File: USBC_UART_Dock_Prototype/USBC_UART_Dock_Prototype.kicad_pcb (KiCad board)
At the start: 4 copper layers, 54.1 x 45.5 mm, 40 parts, among them J1 Conn_01x01, J2 Conn_01x01, J3 Conn_01x05_Socket, J4 USB4085-GF-A, U1 FT312D, U2 TPS25810, U3 TPD6S300A, U5 LP5907MFX-3.3/NOPB, Y1 12 MHz

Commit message: Ready for DFM
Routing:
- net /RTS: track 35.8 -> 31.1 mm
- net /CTS: track 34.7 -> 30.4 mm
- net /nPWR_FLT: track 32.0 -> 27.9 mm, vias 0 -> 2
- net /CONN_USB_CC2: track 12.3 -> 16.4 mm
- net GND: track 23.7 -> 27.2 mm
- net +3.3V: track 25.7 -> 22.2 mm, vias 23 -> 25
- net /nUSB_ERROR: track 44.3 -> 42.8 mm
- net +VUSB: track 5.74 -> 4.39 mm
- net Net-(U3-VBIAS): track 8.47 -> 7.48 mm, vias 2 -> 0
- net /nLD_DET: track 5.26 -> 5.97 mm
- net Net-(D5-A): track 4.28 -> 3.70 mm

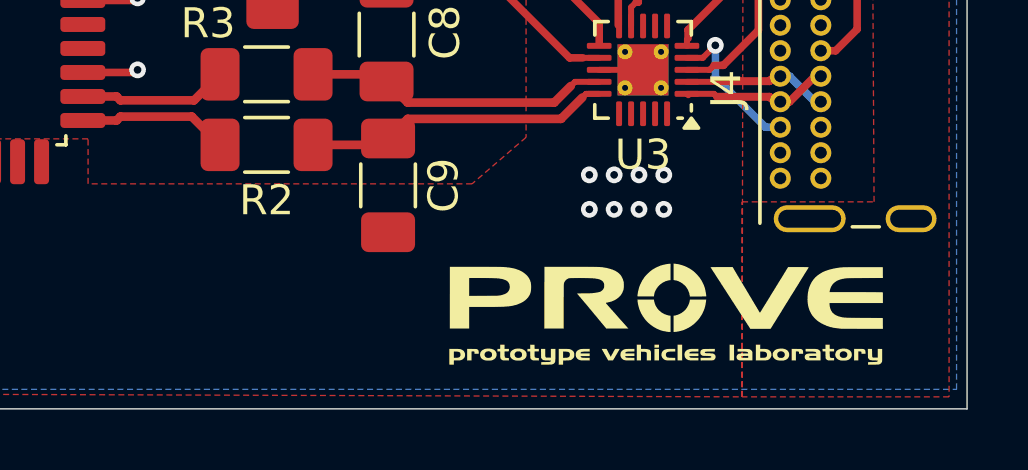
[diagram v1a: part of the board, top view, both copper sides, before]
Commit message: Add BAC logo
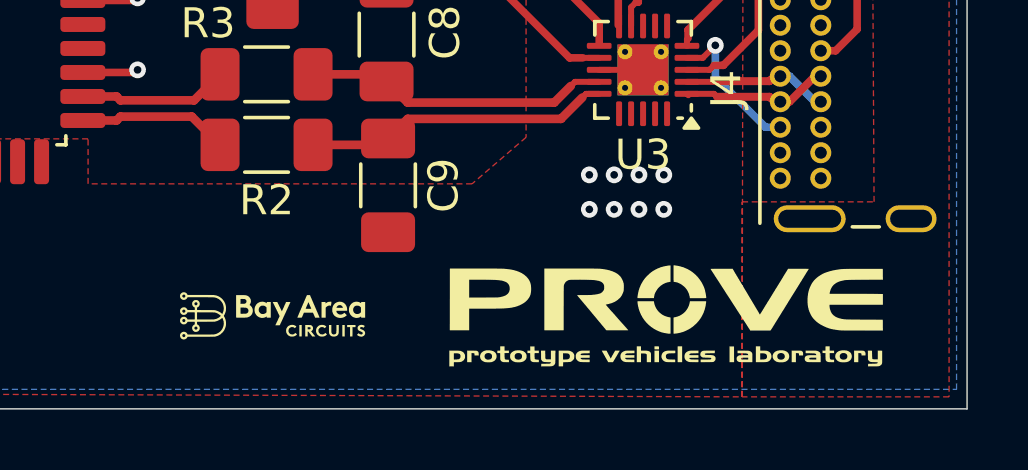
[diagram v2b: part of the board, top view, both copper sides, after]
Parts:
- added G***: LOGO, PROVE:BAC-logo, F.Cu at (145.9, 101.9)
- moved G*** 0.06 mm to (159.0, 102.1)
